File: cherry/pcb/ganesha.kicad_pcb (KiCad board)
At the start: 4 copper layers, 4.4 x 4.6 mm, 124 parts, among them J1 MJ-4PP-9, J2 Conn_01x04, SW1 SW_PUSH, SW10 SW_PUSH, SW11 SW_PUSH, SW12 SW_PUSH, SW13 SW_PUSH, SW14 SW_PUSH, SW15 SW_PUSH, SW16 SW_PUSH, SW17 SW_PUSH, SW18 SW_PUSH, SW19 SW_PUSH, SW2 SW_PUSH, SW20 SW_PUSH, SW21 SW_PUSH, SW22 SW_PUSH, SW23 SW_PUSH, SW24 SW_PUSH, SW25 SW_PUSH, SW26 SW_PUSH, SW27 SW_PUSH, SW28 SW_PUSH, SW3 SW_PUSH, SW4 SW_PUSH, SW5 SW_PUSH, SW6 SW_PUSH, SW7 SW_PUSH, SW8 SW_PUSH, SW9 SW_PUSH, U2 MIC5219-2.5YM5, U3 ATmega32U4-AU, Y1 16MHz

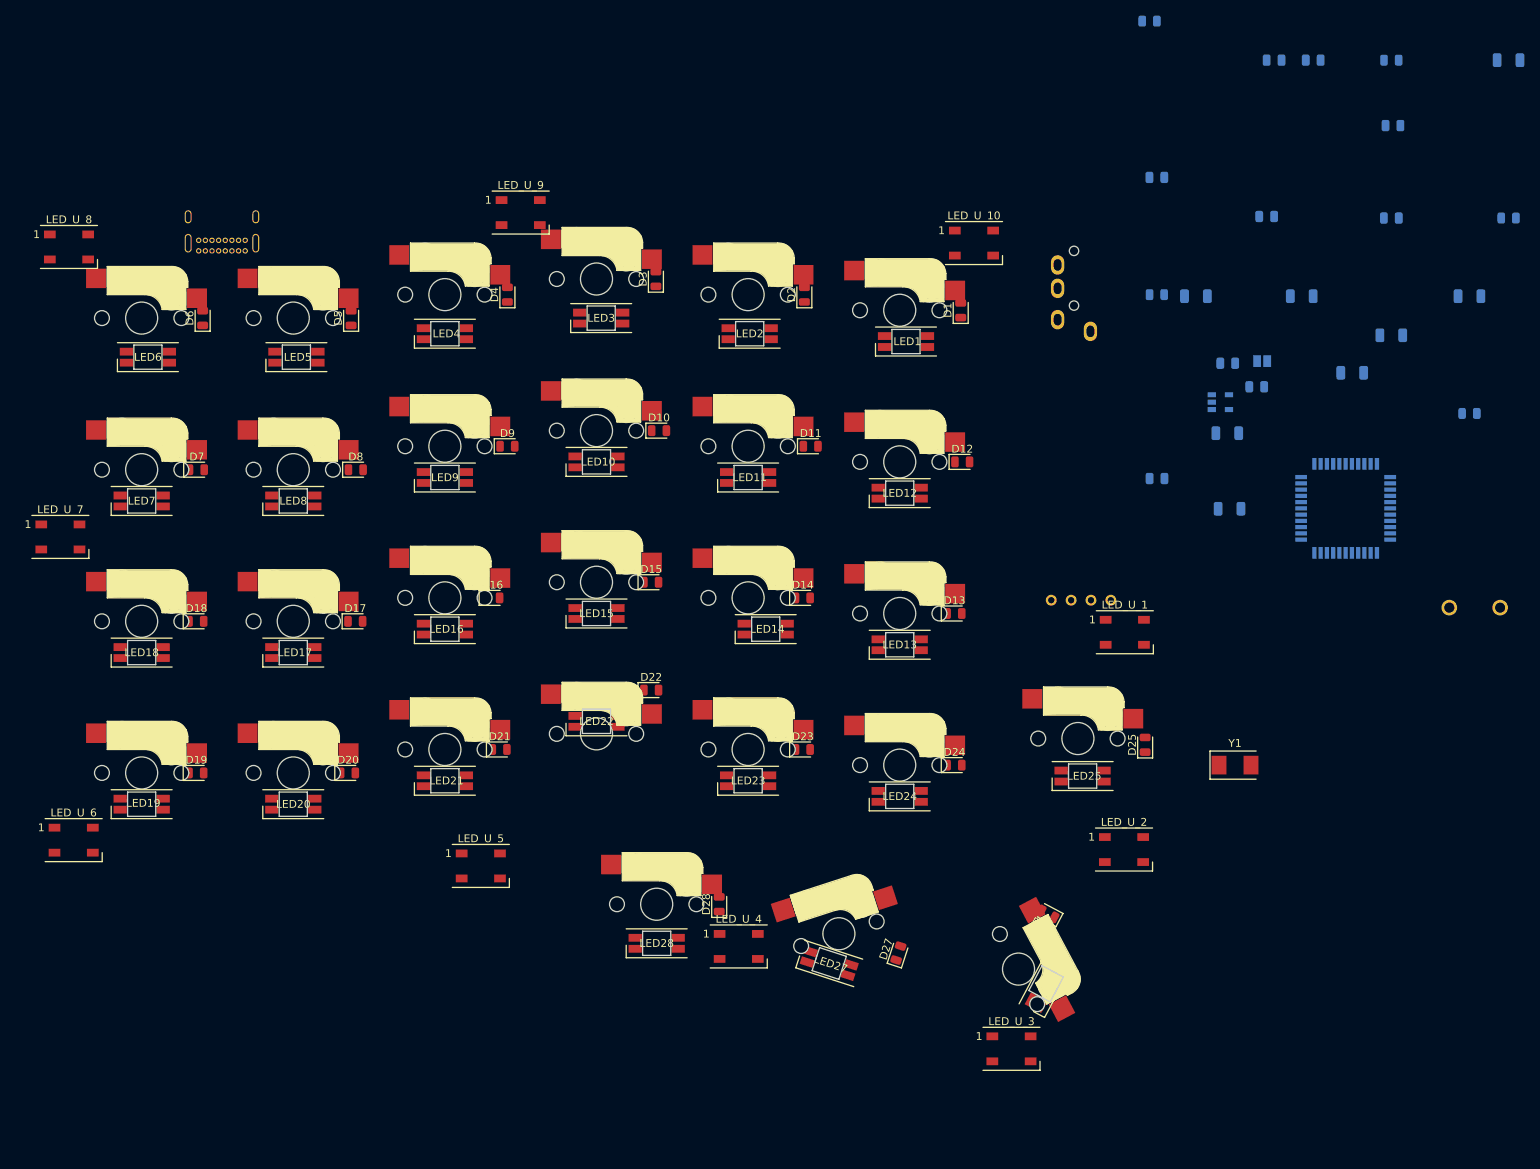
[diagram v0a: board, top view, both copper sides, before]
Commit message: Tightened up layout. Added rough cut edge.
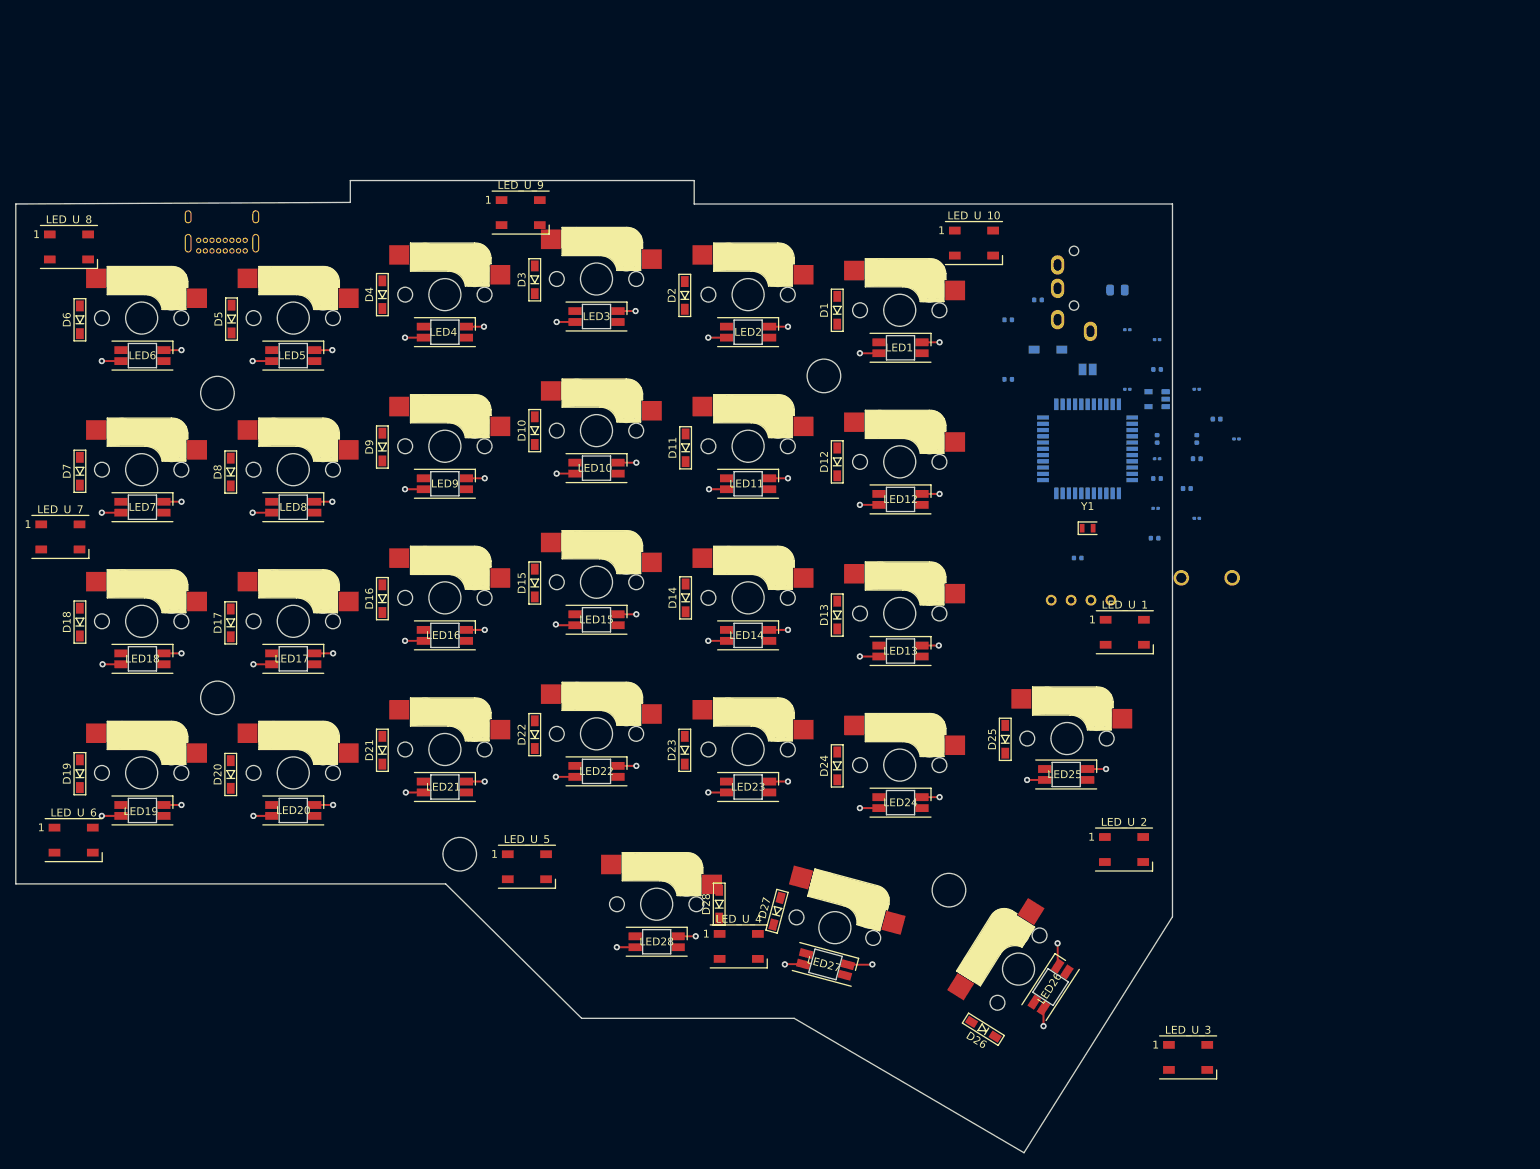
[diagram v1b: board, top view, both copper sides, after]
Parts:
- added Ref**: Val**, kbd:M2_HOLE_v2, F.Cu at (197.4, 40.2)
- added Ref**: Val**, kbd:M2_HOLE_v2, F.Cu at (119.8, 42.4)
- added Ref**: Val**, kbd:M2_HOLE_v2, F.Cu at (119.8, 81.4)
- added Ref**: Val**, kbd:M2_HOLE_v2, F.Cu at (150.8, 101.4)
- added Ref**: Val**, kbd:M2_HOLE_v2, F.Cu at (213.4, 106.0)
- C1, C10, C13, C19, C2, C3, C4, C5, C6: footprint Capacitor_SMD:C_0805_2012Metric -> Capacitor_SMD:C_0402_1005Metric
- D1, D10, D11, D12, D13, D14, D15, D16, D17, D18, D19, D2, D20, D21, D22, D23, D24, D25, D26, D27, D28, D3, D4, D5, D57, D6, D7, D8, D9: footprint Diode_SMD:D_0805_2012Metric -> kbd:D3_SMD_v2
- LED_G1, LED_R1, LED_Y1: footprint LED_SMD:LED_0805_2012Metric -> LED_SMD:LED_0402_1005Metric
- R11, R2, R4, R5, R6, R7, R8, R9: footprint Resistor_SMD:R_1206_3216Metric -> Resistor_SMD:R_0201_0603Metric
- Y1: footprint Crystal:Crystal_SMD_Abracon_ABM3-2Pin_5.0x3.2mm -> Crystal:Crystal_SMD_2012-2Pin_2.0x1.2mm
- moved R4 68.0 mm to (240.0, 50.8)
- moved LED_G1 60.0 mm to (243.8, 54.6), turned to 180 degrees
- moved C2 56.5 mm to (221.0, 40.6), turned to 180 degrees
- moved LED_R1 51.1 mm to (247.7, 45.7)
- moved F1 50.9 mm to (234.9, 29.2)
- moved C19 50.6 mm to (224.8, 30.5), turned to 180 degrees
- moved C6 47.5 mm to (221.0, 33.0)
- moved C4 46.2 mm to (239.7, 61.0)
- moved R9 40.4 mm to (240.0, 35.6)
- moved C10 37.7 mm to (245.1, 48.3), turned to 270 degrees
- moved Y1 35.7 mm to (231.1, 59.7)
- moved LED_Y1 35.4 mm to (245.1, 50.8), turned to 180 degrees
- moved RSW1 34.5 mm to (246.4, 66.0)
- moved R2 34.2 mm to (245.1, 58.4), turned to 180 degrees
- moved U3 33.9 mm to (231.1, 49.5), turned to 180 degrees
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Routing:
- net VCC: track 0.00 -> 66.6 mm, vias 0 -> 28
- net GND: track 0.00 -> 65.8 mm, vias 0 -> 28
- added copper zone on In2.Cu, net GND
- added copper zone on In1.Cu, net VCC
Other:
- board size 4.4 x 4.6 mm -> 148 x 124.4 mm
